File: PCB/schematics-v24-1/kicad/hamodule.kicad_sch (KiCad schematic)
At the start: 178 parts, among them J1 GND|5V, J10 Tx|Rx, J11 Sda|Scl, J12 3|9, J13 13|12, J14 3.3v|GND|7|15, J15 2604-1104, J16 2604-1104, J17 TestPoint, J19 TestPoint, J2 2604-1102, J3 USB_C_Receptacle_USB2.0, J4 GND|3.3V, J5 Conn_01x02_Pin, J6 2604-1104, J7 2604-1104, J8 5v|GND|Do, J9 Screen, K1 AQG22205, K2 AQG22205, K3 AQG22205, K4 AQG22205, K5 AQG22205, K6 AQG22205, K7 AQG22205, K8 AQG22205, SW1 USB | PS, SW2 Reset, SW3 Boot, U1 LD1117AV33, U10 SN74LV1T34DBV, U11 ULN2803A, U12 TCAL6416, U2 USBLC6-2SC6, U3 ESP32-S3-WROOM-2, U4 LDA210-PDIP, U5 LDA210-PDIP, U6 LDA210-PDIP, U7 LDA210-PDIP, U8 SHT4x, U9 TXB0108PW

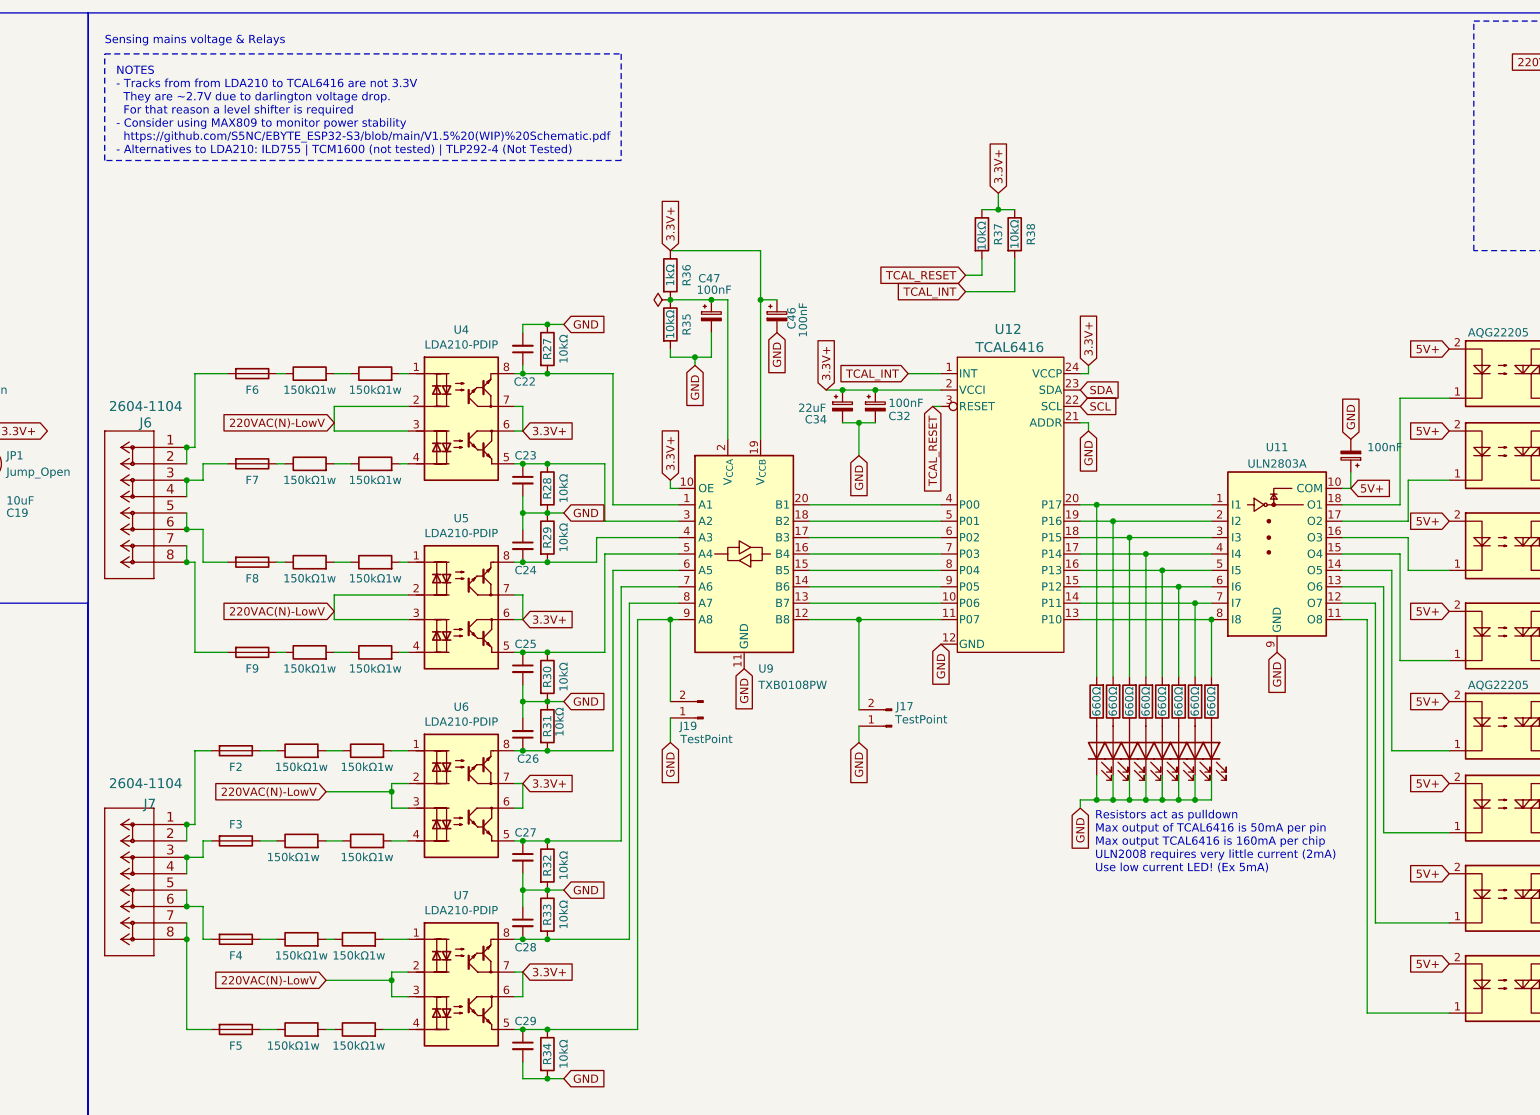
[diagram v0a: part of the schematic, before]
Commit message: adding pull down resistors between I2C and ULN
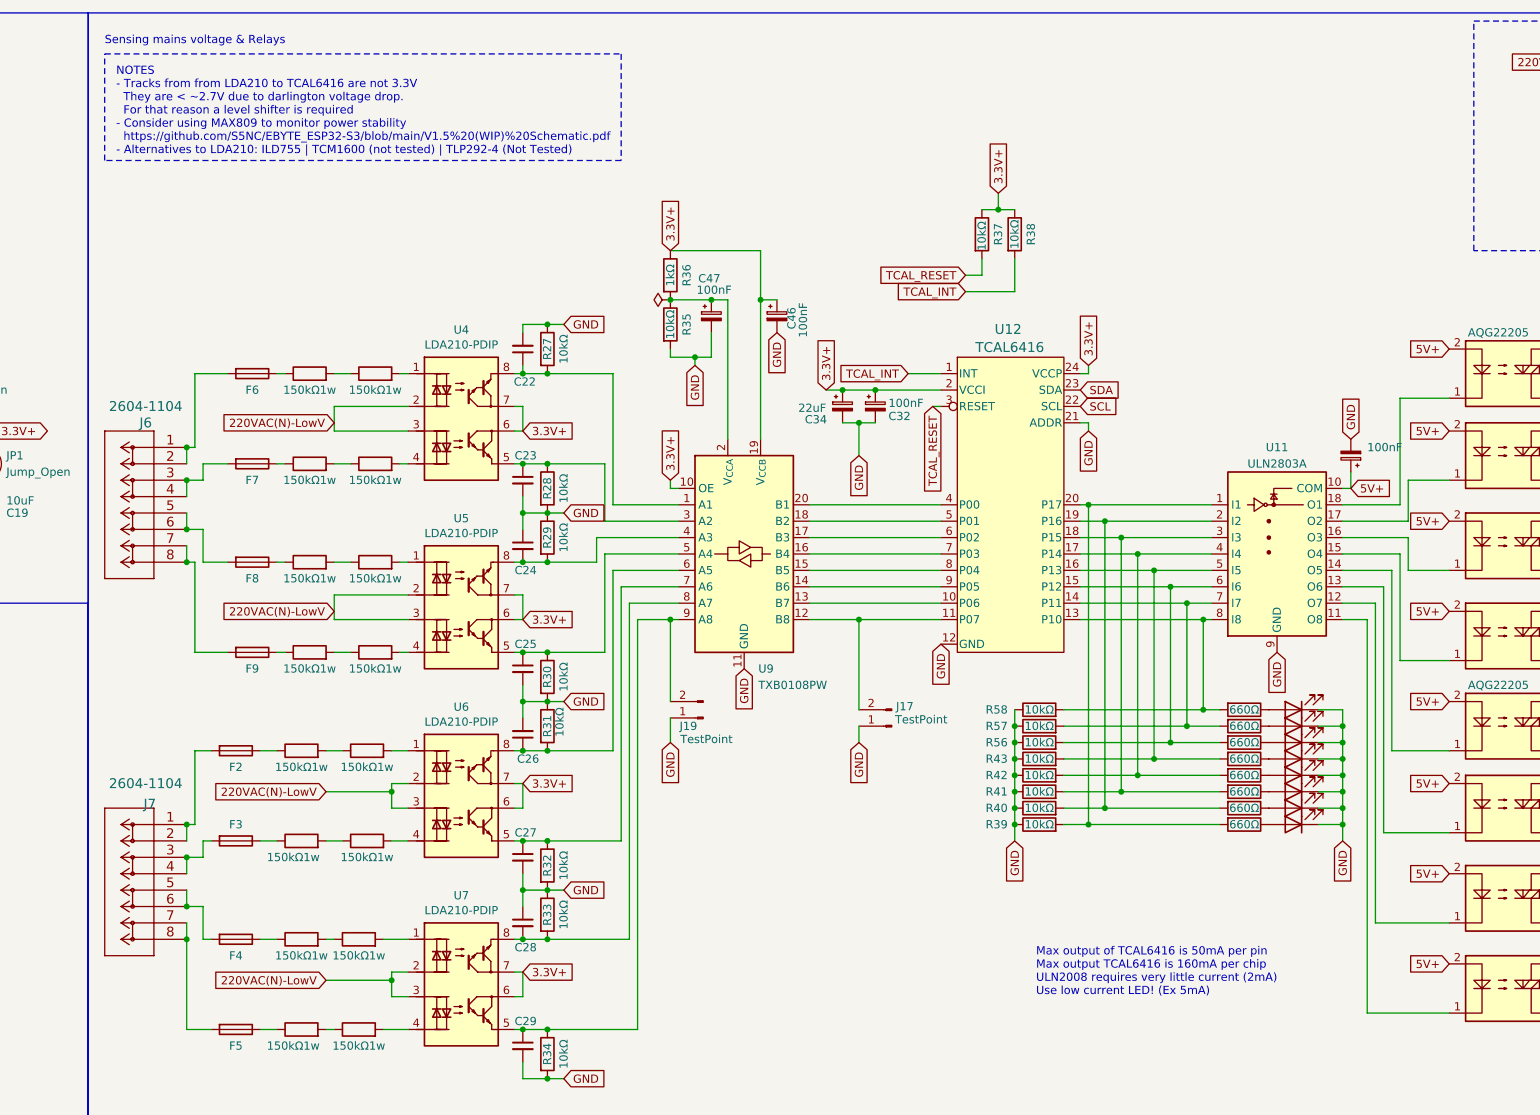
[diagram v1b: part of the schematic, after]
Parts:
- added R39, R40, R41, R42, R43, R56, R57, R58: 10kΩ, Resistor_SMD:R_0603_1608Metric_Pad0.98x0.95mm_HandSolder, symbol Device:R
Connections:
- net GND: now also R39.1, R40.1, R41.1, R42.1, R43.1, R56.1, R57.1, R58.1
- net at R52.2, U11.8 (I8), U12.13 (P10): now also R58.2
- net at R51.2, U11.7 (I7), U12.14 (P11): now also R57.2
- net at R50.2, U11.6 (I6), U12.15 (P12): now also R56.2
- net at R49.2, U11.5 (I5), U12.16 (P13): now also R43.2
- net at R48.2, U11.4 (I4), U12.17 (P14): now also R42.2
- net at R47.2, U11.3 (I3), U12.18 (P15): now also R41.2
- net at R46.2, U11.2 (I2), U12.19 (P16): now also R40.2
- net at R45.2, U11.1 (I1), U12.20 (P17): now also R39.2
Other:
- note added: "Max output of TCAL6416 is 50mA per pin Max output TCAL6416 is 160mA per chip ULN2008 requires very little current (2mA) Use low current LED! (Ex 5mA)"
- note added: "NOTES - Tracks from from LDA210 to TCAL6416 are not 3.3V They are < ~2.7V due to darlington voltage drop. For that reason a level shifter is required - Consider using MAX809 to monitor power stability https://github.com/S5NC/EBYTE_ESP32-S3/blob/main/V1.5%20(WIP)%20Schematic.pdf - Alternatives to LDA210: ILD755 | TCM1600 (not tested) | TLP292-4 (Not Tested)"
- note removed: "NOTES - Tracks from from LDA210 to TCAL6416 are not 3.3V They are ~2.7V due to darlington voltage drop. For that reason a level shifter is required - Consider using MAX809 to monitor power stability https://github.com/S5NC/EBYTE_ESP32-S3/blob/main/V1.5%20(WIP)%20Schematic.pdf - Alternatives to LDA210: ILD755 | TCM1600 (not tested) | TLP292-4 (Not Tested)"
- note removed: "Resistors act as pulldown Max output of TCAL6416 is 50mA per pin Max output TCAL6416 is 160mA per chip ULN2008 requires very little current (2mA) Use low current LED! (Ex 5mA)"
